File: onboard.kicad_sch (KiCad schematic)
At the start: 13 parts, among them Q2 BSS83P, Q3 BSS83P, SW3 SW_DIP_x08, SW4 User, U6 157119S12801, U7 157119S12801

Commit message: WIP: display
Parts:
- added U7: DC56-11CGKWA, Display_7Segment:DA56-11CGKWA, symbol Display_Character:DC56-11CGKWA
- SW3: footprint Button_Switch_SMD:SW_DIP_SPSTx08_Slide_Omron_A6H-8101_W6.15mm_P1.27mm -> Button_Switch_SMD:SW_DIP_SPSTx08_Slide_KingTek_DSHP08TS_W7.62mm_P1.27mm
- renumbered U7 to U8
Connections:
- net +3V3: now also Q2.2 (S), Q3.2 (S); no longer Q2.3 (D), Q3.3 (D)
- net Dig: no longer SW4.1
- net nDig: now also Q2.3 (D); no longer Q2.2 (S)
- net ~{nDig}: now also Q3.3 (D), SW4.1; no longer Q3.2 (S)
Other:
- moved on the sheet: Q2, Q3
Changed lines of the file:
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@@
   (junction (at 139.7 57.15) (diameter 0) (color 0 0 0 0)
   )
-  (junction (at 139.7 88.9) (diameter 0) (color 0 0 0 0)
-  )
   (junction (at 139.7 64.77) (diameter 0) (color 0 0 0 0)
   )
@@
     (stroke (width 0) (type default) (color 0 0 0 0))
   )
-  (wire (pts (xy 139.7 88.9) (xy 139.7 101.6))
+  (wire (pts (xy 139.7 72.39) (xy 139.7 101.6))
     (stroke (width 0) (type default) (color 0 0 0 0))
   )
@@
     (stroke (width 0) (type default) (color 0 0 0 0))
   )
+  (wire (pts (xy 142.24 88.9) (xy 147.32 88.9))
+    (stroke (width 0) (type default) (color 0 0 0 0))
+  )
   (wire (pts (xy 139.7 67.31) (xy 144.78 67.31))
     (stroke (width 0) (type default) (color 0 0 0 0))
@@
     (stroke (width 0) (type default) (color 0 0 0 0))
   )
-  (wire (pts (xy 139.7 88.9) (xy 147.32 88.9))
-    (stroke (width 0) (type default) (color 0 0 0 0))
-  )
   (bus (pts (xy 76.2 62.23) (xy 76.2 64.77))
     (stroke (width 0) (type default) (color 0 0 0 0))
@@
   )
   (wire (pts (xy 78.74 153.67) (xy 93.98 153.67))
-    (stroke (width 0) (type default) (color 0 0 0 0))
-  )
-  (wire (pts (xy 139.7 72.39) (xy 139.7 88.9))
     (stroke (width 0) (type default) (color 0 0 0 0))
   )
@@
   )
   (label "SegR.5" (at 81.28 106.68 0)
+    (effects (font (size 1.27 1.27)) (justify left bottom))
+  )
+  (label "~{nDig}" (at 142.24 88.9 0)
     (effects (font (size 1.27 1.27)) (justify left bottom))
   )
@@
     (pin "1")
   )
+  (symbol (lib_id "Display_Character:DC56-11CGKWA") (at 39.37 115.57 0) (unit 1)
+    (in_bom yes) (on_board yes) (fields_autoplaced)
+    (property "Reference" "U7" (id 0) (at 39.37 97.79 0))
+    (property "Value" "DC56-11CGKWA" (id 1) (at 39.37 100.33 0))
+    (property "Footprint" "Display_7Segment:DA56-11CGKWA" (id 2) (at 39.878 132.08 0)
+      (effects (font (size 1.27 1.27)) hide)
+    )
+    (property "Datasheet" "http://www.kingbright.com/attachments/file/psearch/000/00/00/DC56-11CGKWA(Ver.7A).pdf" (id 3) (at 36.322 113.03 0)
+      (effects (font (size 1.27 1.27)) hide)
+    )
+    (pin "1")
+    (pin "10")
+    (pin "11")
+    (pin "12")
+    (pin "13")
+    (pin "14")
+    (pin "15")
+    (pin "16")
+    (pin "17")
+    (pin "18")
+    (pin "2")
+    (pin "3")
+    (pin "4")
+    (pin "5")
+    (pin "6")
+    (pin "7")
+    (pin "8")
+    (pin "9")
+  )
   (symbol (lib_id "Device:R") (at 177.8 162.56 0) (mirror y) (unit 1)
     (in_bom yes) (on_board yes)
@@
     (pin "8")
   )
-  (symbol (lib_id "Transistor_FET:BSS83P") (at 180.34 143.51 0) (mirror y) (unit 1)
+  (symbol (lib_id "Transistor_FET:BSS83P") (at 180.34 143.51 180) (unit 1)
     (in_bom yes) (on_board yes) (fields_autoplaced)
     (property "Reference" "Q2" (id 0) (at 173.99 142.2399 0)
@@
       (effects (font (size 1.27 1.27)) (justify left))
     )
-    (property "Footprint" "Package_TO_SOT_SMD:SOT-23" (id 2) (at 175.26 145.415 0)
+    (property "Footprint" "Package_TO_SOT_SMD:SOT-23" (id 2) (at 175.26 141.605 0)
       (effects (font (size 1.27 1.27) italic) (justify left) hide)
     )
@@
     (property "Reference" "SW3" (id 0) (at 152.4 48.1035 0))
     (property "Value" "SW_DIP_x08" (id 1) (at 152.4 50.8786 0))
-    (property "Footprint" "Button_Switch_SMD:SW_DIP_SPSTx08_Slide_Omron_A6H-8101_W6.15mm_P1.27mm" (id 2) (at 152.4 64.77 0)
+    (property "Footprint" "Button_Switch_SMD:SW_DIP_SPSTx08_Slide_KingTek_DSHP08TS_W7.62mm_P1.27mm" (id 2) (at 152.4 64.77 0)
       (effects (font (size 1.27 1.27)) hide)
     )
@@
   (symbol (lib_id "Display_Character:SA39-11EWA") (at 101.6 146.05 0) (unit 1)
     (in_bom yes) (on_board yes)
-    (property "Reference" "U7" (id 0) (at 101.6 129.54 0))
+    (property "Reference" "U8" (id 0) (at 101.6 129.54 0))
     (property "Value" "157119S12801" (id 1) (at 101.6 132.08 0))
     (property "Footprint" "Display_7Segment:Sx39-1xxxxx" (id 2) (at 101.6 160.02 0)
@@
     (pin "2")
   )
-  (symbol (lib_id "Transistor_FET:BSS83P") (at 154.94 148.59 0) (mirror y) (unit 1)
+  (symbol (lib_id "Transistor_FET:BSS83P") (at 154.94 148.59 180) (unit 1)
     (in_bom yes) (on_board yes) (fields_autoplaced)
     (property "Reference" "Q3" (id 0) (at 148.59 147.3199 0)
@@
       (effects (font (size 1.27 1.27)) (justify left))
     )
-    (property "Footprint" "Package_TO_SOT_SMD:SOT-23" (id 2) (at 149.86 150.495 0)
+    (property "Footprint" "Package_TO_SOT_SMD:SOT-23" (id 2) (at 149.86 146.685 0)
       (effects (font (size 1.27 1.27) italic) (justify left) hide)
     )

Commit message: Done. I hope.
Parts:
- removed U7: DC56-11CGKWA, Display_7Segment:DA56-11CGKWA, symbol Display_Character:DC56-11CGKWA
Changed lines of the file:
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@@
     (pin "1")
-  )
-  (symbol (lib_id "Display_Character:DC56-11CGKWA") (at 39.37 115.57 0) (unit 1)
-    (in_bom yes) (on_board yes) (fields_autoplaced)
-    (property "Reference" "U7" (id 0) (at 39.37 97.79 0))
-    (property "Value" "DC56-11CGKWA" (id 1) (at 39.37 100.33 0))
-    (property "Footprint" "Display_7Segment:DA56-11CGKWA" (id 2) (at 39.878 132.08 0)
-      (effects (font (size 1.27 1.27)) hide)
-    )
-    (property "Datasheet" "http://www.kingbright.com/attachments/file/psearch/000/00/00/DC56-11CGKWA(Ver.7A).pdf" (id 3) (at 36.322 113.03 0)
-      (effects (font (size 1.27 1.27)) hide)
-    )
-    (pin "1")
-    (pin "10")
-    (pin "11")
-    (pin "12")
-    (pin "13")
-    (pin "14")
-    (pin "15")
-    (pin "16")
-    (pin "17")
-    (pin "18")
-    (pin "2")
-    (pin "3")
-    (pin "4")
-    (pin "5")
-    (pin "6")
-    (pin "7")
-    (pin "8")
-    (pin "9")
   )
   (symbol (lib_id "Device:R") (at 177.8 162.56 0) (mirror y) (unit 1)

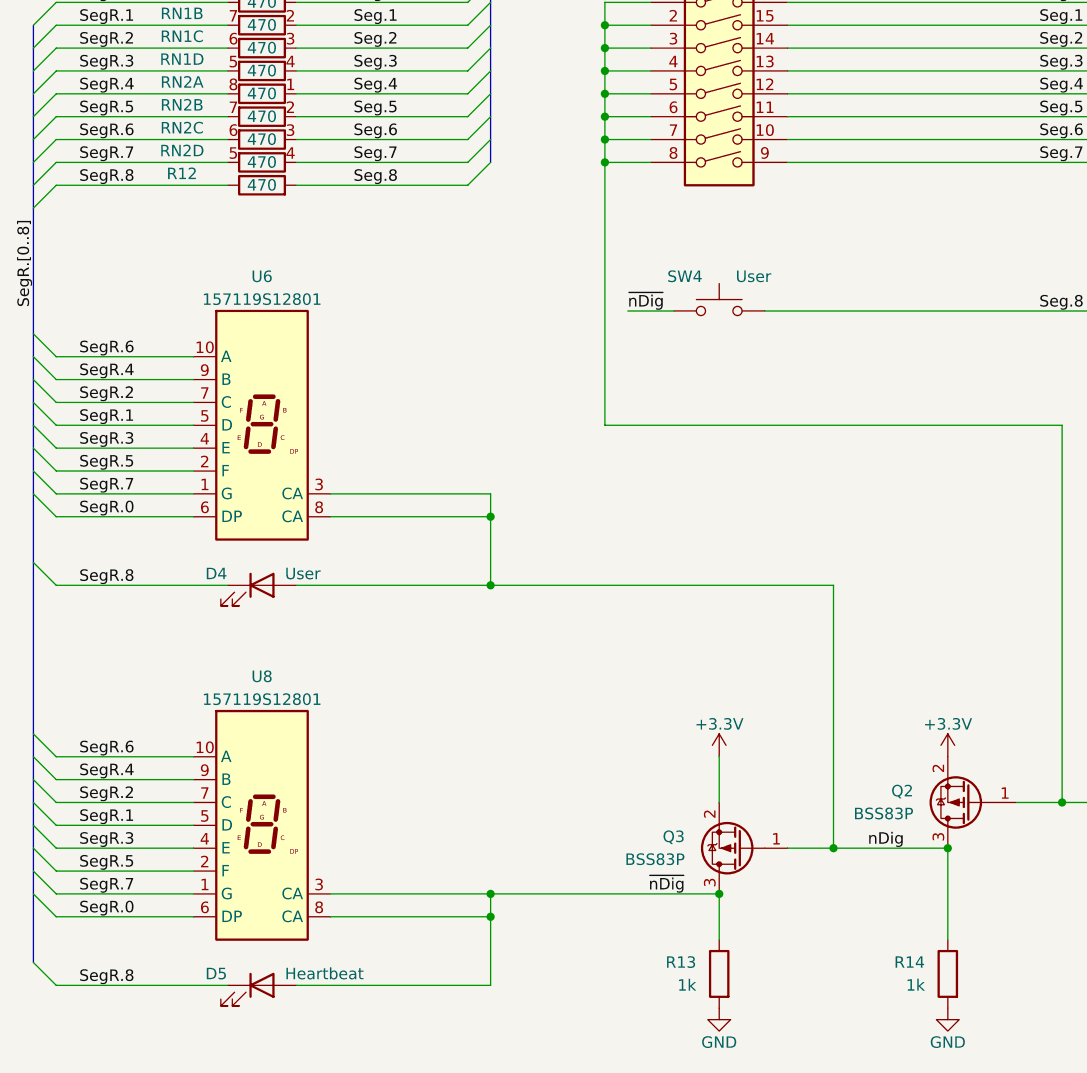
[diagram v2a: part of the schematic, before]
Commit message: rev1.1: Add I2C pullups
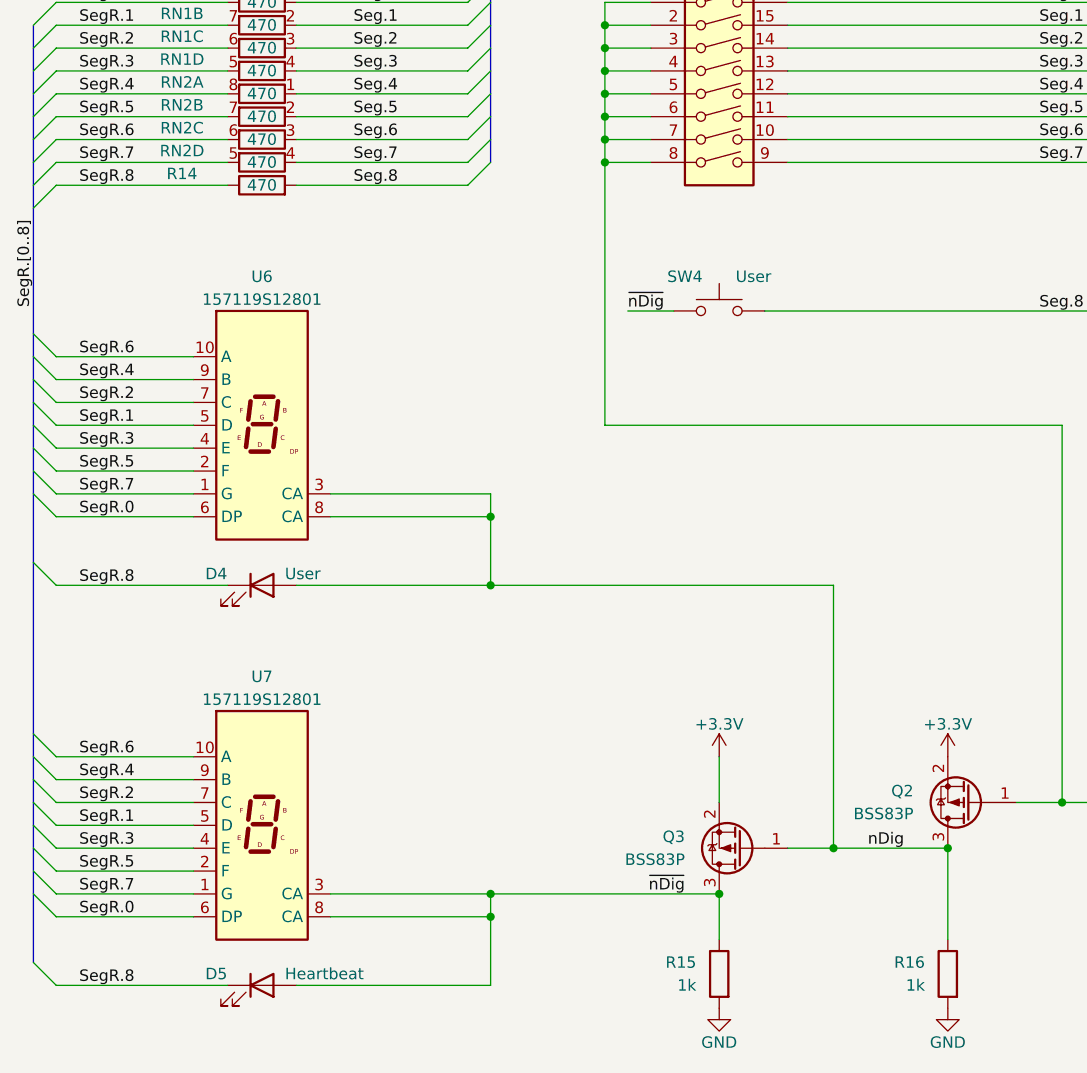
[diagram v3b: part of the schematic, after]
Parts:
- renumbered R12 to R14, R13 to R15, R14 to R16, U8 to U7
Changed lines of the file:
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@@
   (title_block
     (title "[canbrd] CAN/RS485 IO board")
-    (date "2022-02-24")
-    (rev "1.0")
+    (date "2022-03-18")
+    (rev "1.1")
   )
   (junction (at 139.7 62.23) (diameter 0) (color 0 0 0 0)
@@
   (symbol (lib_id "power:+3.3V") (at 177.8 138.43 0) (mirror y) (unit 1)
     (in_bom yes) (on_board yes) (fields_autoplaced)
-    (property "Reference" "#PWR052" (id 0) (at 177.8 142.24 0)
+    (property "Reference" "#PWR054" (id 0) (at 177.8 142.24 0)
       (effects (font (size 1.27 1.27)) hide)
     )
@@
   (symbol (lib_id "Device:R") (at 177.8 162.56 0) (mirror y) (unit 1)
     (in_bom yes) (on_board yes)
-    (property "Reference" "R14" (id 0) (at 175.26 161.29 0)
+    (property "Reference" "R16" (id 0) (at 175.26 161.29 0)
       (effects (font (size 1.27 1.27)) (justify left))
     )
@@
   (symbol (lib_id "power:GND") (at 177.8 166.37 0) (mirror y) (unit 1)
     (in_bom yes) (on_board yes)
-    (property "Reference" "#PWR054" (id 0) (at 177.8 172.72 0)
+    (property "Reference" "#PWR056" (id 0) (at 177.8 172.72 0)
       (effects (font (size 1.27 1.27)) hide)
     )
@@
   (symbol (lib_id "power:+3.3V") (at 152.4 138.43 0) (mirror y) (unit 1)
     (in_bom yes) (on_board yes) (fields_autoplaced)
-    (property "Reference" "#PWR051" (id 0) (at 152.4 142.24 0)
+    (property "Reference" "#PWR053" (id 0) (at 152.4 142.24 0)
       (effects (font (size 1.27 1.27)) hide)
     )
@@
   (symbol (lib_id "Display_Character:SA39-11EWA") (at 101.6 146.05 0) (unit 1)
     (in_bom yes) (on_board yes)
-    (property "Reference" "U8" (id 0) (at 101.6 129.54 0))
+    (property "Reference" "U7" (id 0) (at 101.6 129.54 0))
     (property "Value" "157119S12801" (id 1) (at 101.6 132.08 0))
     (property "Footprint" "Display_7Segment:Sx39-1xxxxx" (id 2) (at 101.6 160.02 0)
@@
   (symbol (lib_id "Device:R") (at 101.6 74.93 90) (unit 1)
     (in_bom yes) (on_board yes)
-    (property "Reference" "R12" (id 0) (at 92.71 73.66 90))
+    (property "Reference" "R14" (id 0) (at 92.71 73.66 90))
     (property "Value" "470" (id 1) (at 101.6 74.93 90))
     (property "Footprint" "Resistor_SMD:R_0603_1608Metric" (id 2) (at 101.6 76.708 90)
@@
   (symbol (lib_id "power:GND") (at 152.4 166.37 0) (mirror y) (unit 1)
     (in_bom yes) (on_board yes)
-    (property "Reference" "#PWR053" (id 0) (at 152.4 172.72 0)
+    (property "Reference" "#PWR055" (id 0) (at 152.4 172.72 0)
       (effects (font (size 1.27 1.27)) hide)
     )
@@
   (symbol (lib_id "Device:R") (at 152.4 162.56 0) (mirror y) (unit 1)
     (in_bom yes) (on_board yes)
-    (property "Reference" "R13" (id 0) (at 149.86 161.29 0)
+    (property "Reference" "R15" (id 0) (at 149.86 161.29 0)
       (effects (font (size 1.27 1.27)) (justify left))
     )
